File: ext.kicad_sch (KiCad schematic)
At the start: 29 parts, among them J4 0826-1X1T-GH-F, U10 LTC6820IUD, U11 LTC6820IUD, U12 LTC6820IUD, U13 LTC6820IUD

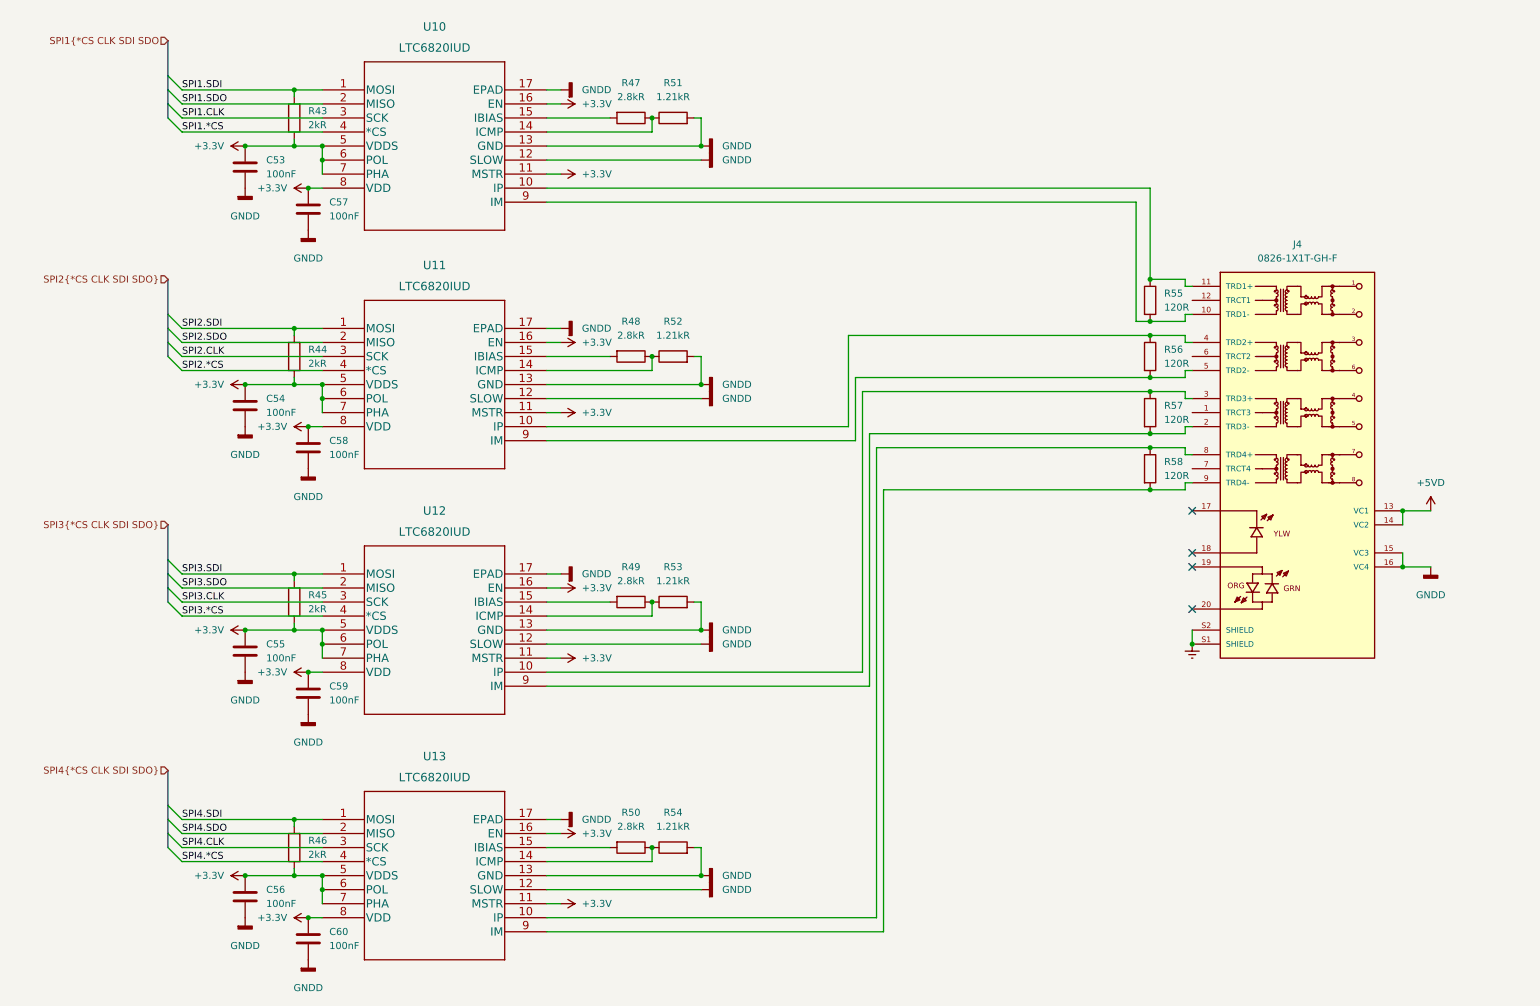
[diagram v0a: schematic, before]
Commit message: Common power stage for field IO
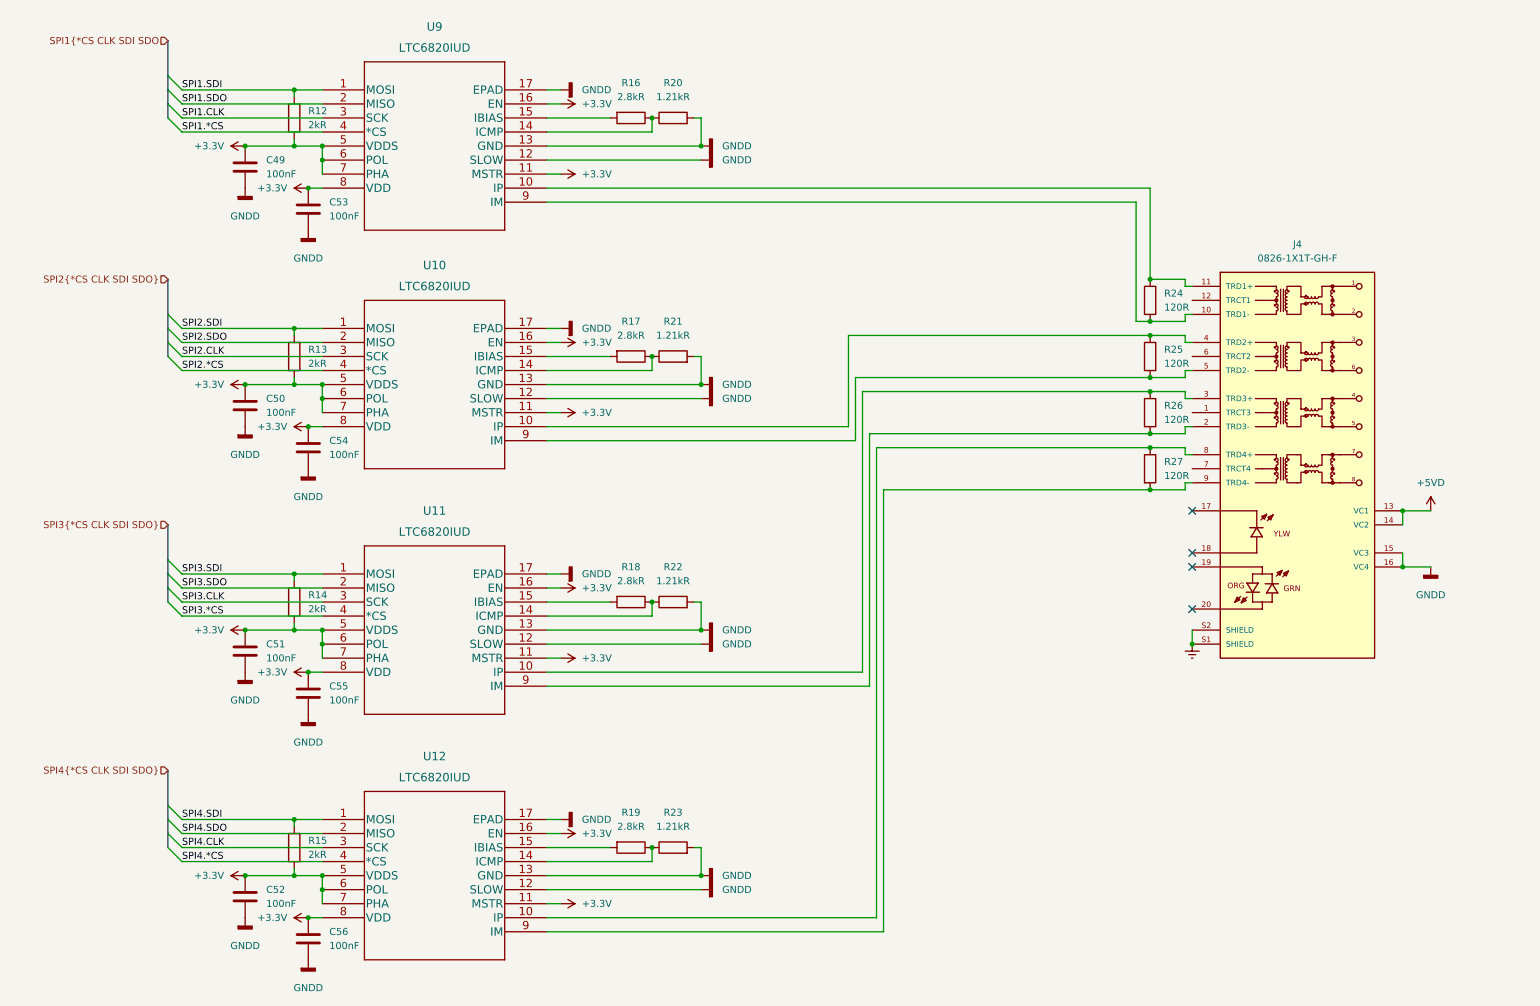
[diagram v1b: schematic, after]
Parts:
- renumbered C53 to C49, C54 to C50, C55 to C51, C56 to C52, C57 to C53, C58 to C54, C59 to C55, C60 to C56, R43 to R12, R44 to R13, R45 to R14, R46 to R15, R47 to R16, R48 to R17, R49 to R18, R50 to R19, R51 to R20, R52 to R21, R53 to R22, R54 to R23, R55 to R24, R56 to R25, R57 to R26, R58 to R27, U11 to U10, U12 to U11, U13 to U12, U10 to U9

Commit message: routing stuff
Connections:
- net TRD1-: now reaches J4.10 (TRD1-), R24.2, U9.9 (IM)
- net TRD1+: now reaches J4.11 (TRD1+), R24.1, U9.10 (IP)
- net TRD3-: now reaches J4.2 (TRD3-), R26.2, U11.9 (IM)
- net TRD3+: now reaches J4.3 (TRD3+), R26.1, U11.10 (IP)
- net TRD2+: now reaches J4.4 (TRD2+), R25.1, U10.10 (IP)
- net TRD2-: now reaches J4.5 (TRD2-), R25.2, U10.9 (IM)
- net TRD4+: now reaches J4.8 (TRD4+), R27.1, U12.10 (IP)
- net TRD4-: now reaches J4.9 (TRD4-), R27.2, U12.9 (IM)
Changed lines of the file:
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@@
+    (effects (font (size 1.27 1.27)) (justify left bottom))
+  )
+  (label "TRD2-" (at 135.89 90.17 0)
     (effects (font (size 1.27 1.27)) (justify left bottom))
   )
@@
     (effects (font (size 1.27 1.27)) (justify left bottom))
   )
+  (label "TRD4+" (at 135.89 176.53 0)
+    (effects (font (size 1.27 1.27)) (justify left bottom))
+  )
   (label "SPI4.*CS" (at 48.26 166.37 0)
     (effects (font (size 1.27 1.27)) (justify left bottom))
@@
   )
   (label "SPI2.SDI" (at 48.26 69.85 0)
+    (effects (font (size 1.27 1.27)) (justify left bottom))
+  )
+  (label "TRD1-" (at 133.35 46.99 0)
+    (effects (font (size 1.27 1.27)) (justify left bottom))
+  )
+  (label "TRD2+" (at 135.89 87.63 0)
     (effects (font (size 1.27 1.27)) (justify left bottom))
   )
@@
     (effects (font (size 1.27 1.27)) (justify left bottom))
   )
+  (label "TRD1+" (at 133.35 44.45 0)
+    (effects (font (size 1.27 1.27)) (justify left bottom))
+  )
+  (label "TRD3+" (at 137.16 132.08 0)
+    (effects (font (size 1.27 1.27)) (justify left bottom))
+  )
+  (label "TRD4-" (at 135.89 179.07 0)
+    (effects (font (size 1.27 1.27)) (justify left bottom))
+  )
   (label "SPI3.CLK" (at 48.26 119.38 0)
     (effects (font (size 1.27 1.27)) (justify left bottom))
@@
     (effects (font (size 1.27 1.27)) (justify left bottom))
   )
+  (label "TRD3-" (at 137.16 134.62 0)
+    (effects (font (size 1.27 1.27)) (justify left bottom))
+  )

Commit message: Basic routing done, cheating a bit on the diff + add holes (to be positionned)
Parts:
- U10, U11, U12, U9: footprint Maxim industrial IO:LTC6820IUD -> QFN-16_UD_AA_ADI
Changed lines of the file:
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@@
     (pin "1")
   )
-  (symbol (lib_name "LTC6820IUD_2") (lib_id "Num-IO:LTC6820IUD") (at 73.66 158.75 0) (unit 1)
+  (symbol (lib_id "Num-IO:LTC6820IUD") (at 73.66 158.75 0) (unit 1)
     (in_bom yes) (on_board yes) (fields_autoplaced)
     (property "Reference" "U12" (id 0) (at 93.98 147.32 0)
@@
       (effects (font (size 1.524 1.524)))
     )
-    (property "Footprint" "Maxim industrial IO:LTC6820IUD" (id 2) (at 93.98 152.654 0)
+    (property "Footprint" "QFN-16_UD_AA_ADI" (id 2) (at 93.98 152.654 0)
       (effects (font (size 1.524 1.524)) hide)
     )
@@
     (pin "2")
   )
-  (symbol (lib_name "LTC6820IUD_1") (lib_id "Num-IO:LTC6820IUD") (at 73.66 114.3 0) (unit 1)
+  (symbol (lib_id "Num-IO:LTC6820IUD") (at 73.66 114.3 0) (unit 1)
     (in_bom yes) (on_board yes) (fields_autoplaced)
     (property "Reference" "U11" (id 0) (at 93.98 102.87 0)
@@
       (effects (font (size 1.524 1.524)))
     )
-    (property "Footprint" "Maxim industrial IO:LTC6820IUD" (id 2) (at 93.98 108.204 0)
+    (property "Footprint" "QFN-16_UD_AA_ADI" (id 2) (at 93.98 108.204 0)
       (effects (font (size 1.524 1.524)) hide)
     )
@@
       (effects (font (size 1.524 1.524)))
     )
-    (property "Footprint" "Maxim industrial IO:LTC6820IUD" (id 2) (at 93.98 63.754 0)
+    (property "Footprint" "QFN-16_UD_AA_ADI" (id 2) (at 93.98 63.754 0)
       (effects (font (size 1.524 1.524)) hide)
     )
@@
     (pin "1")
   )
-  (symbol (lib_name "LTC6820IUD_3") (lib_id "Num-IO:LTC6820IUD") (at 73.66 26.67 0) (unit 1)
+  (symbol (lib_id "Num-IO:LTC6820IUD") (at 73.66 26.67 0) (unit 1)
     (in_bom yes) (on_board yes) (fields_autoplaced)
     (property "Reference" "U9" (id 0) (at 93.98 15.24 0)
@@
       (effects (font (size 1.524 1.524)))
     )
-    (property "Footprint" "Maxim industrial IO:LTC6820IUD" (id 2) (at 93.98 20.574 0)
+    (property "Footprint" "QFN-16_UD_AA_ADI" (id 2) (at 93.98 20.574 0)
       (effects (font (size 1.524 1.524)) hide)
     )

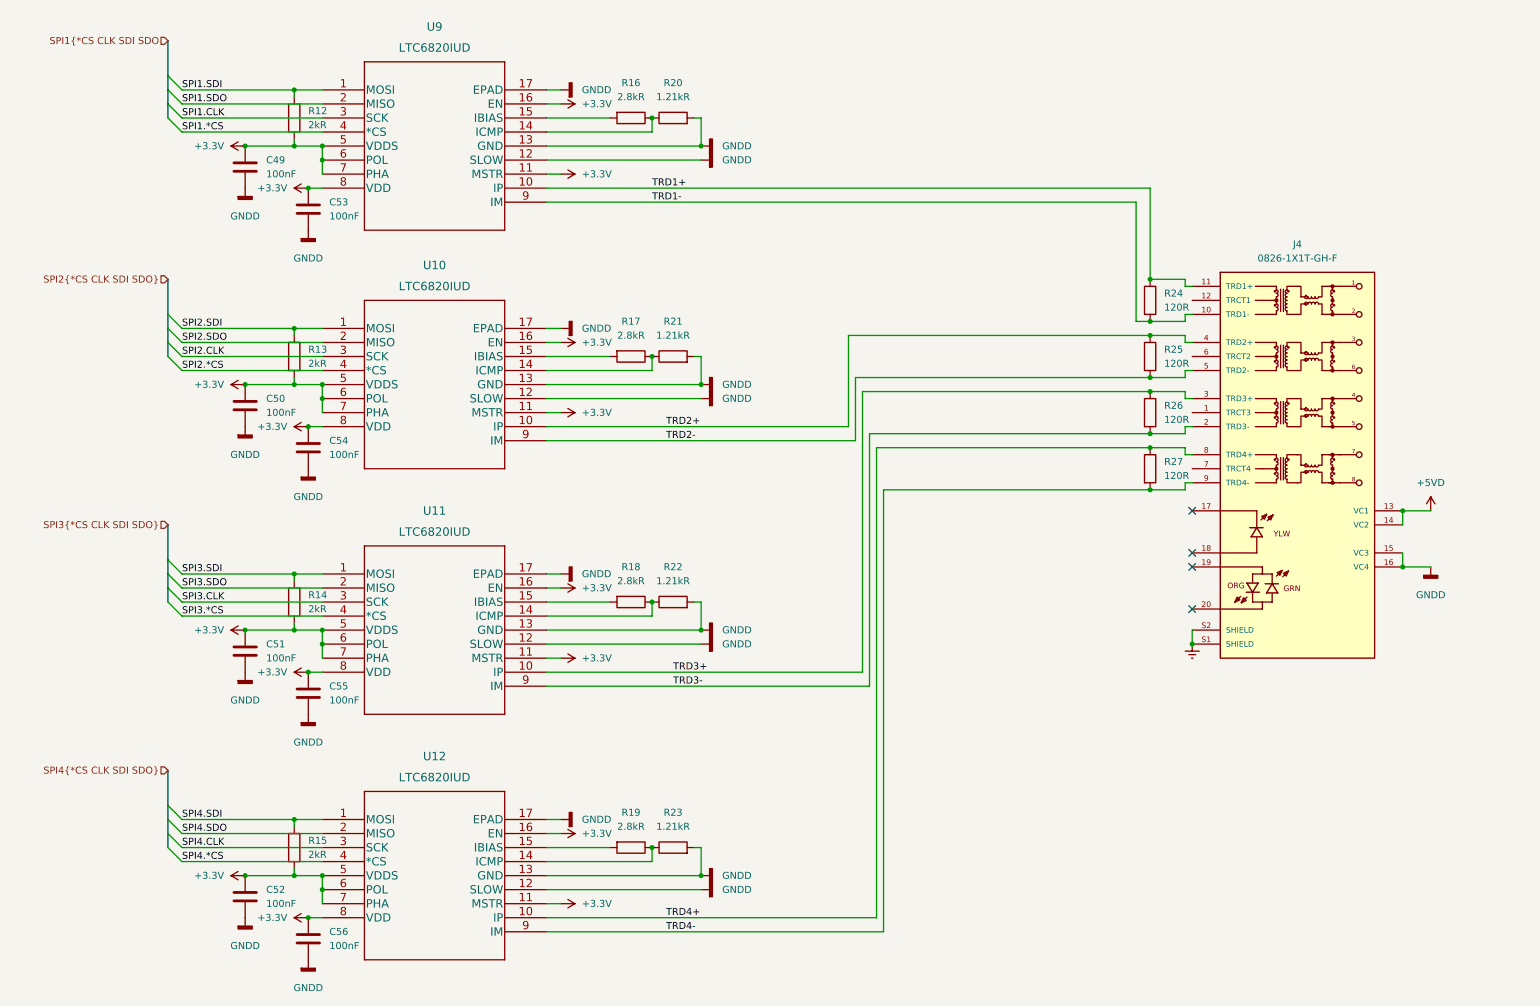
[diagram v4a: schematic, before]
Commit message: change package QFN => MSOP
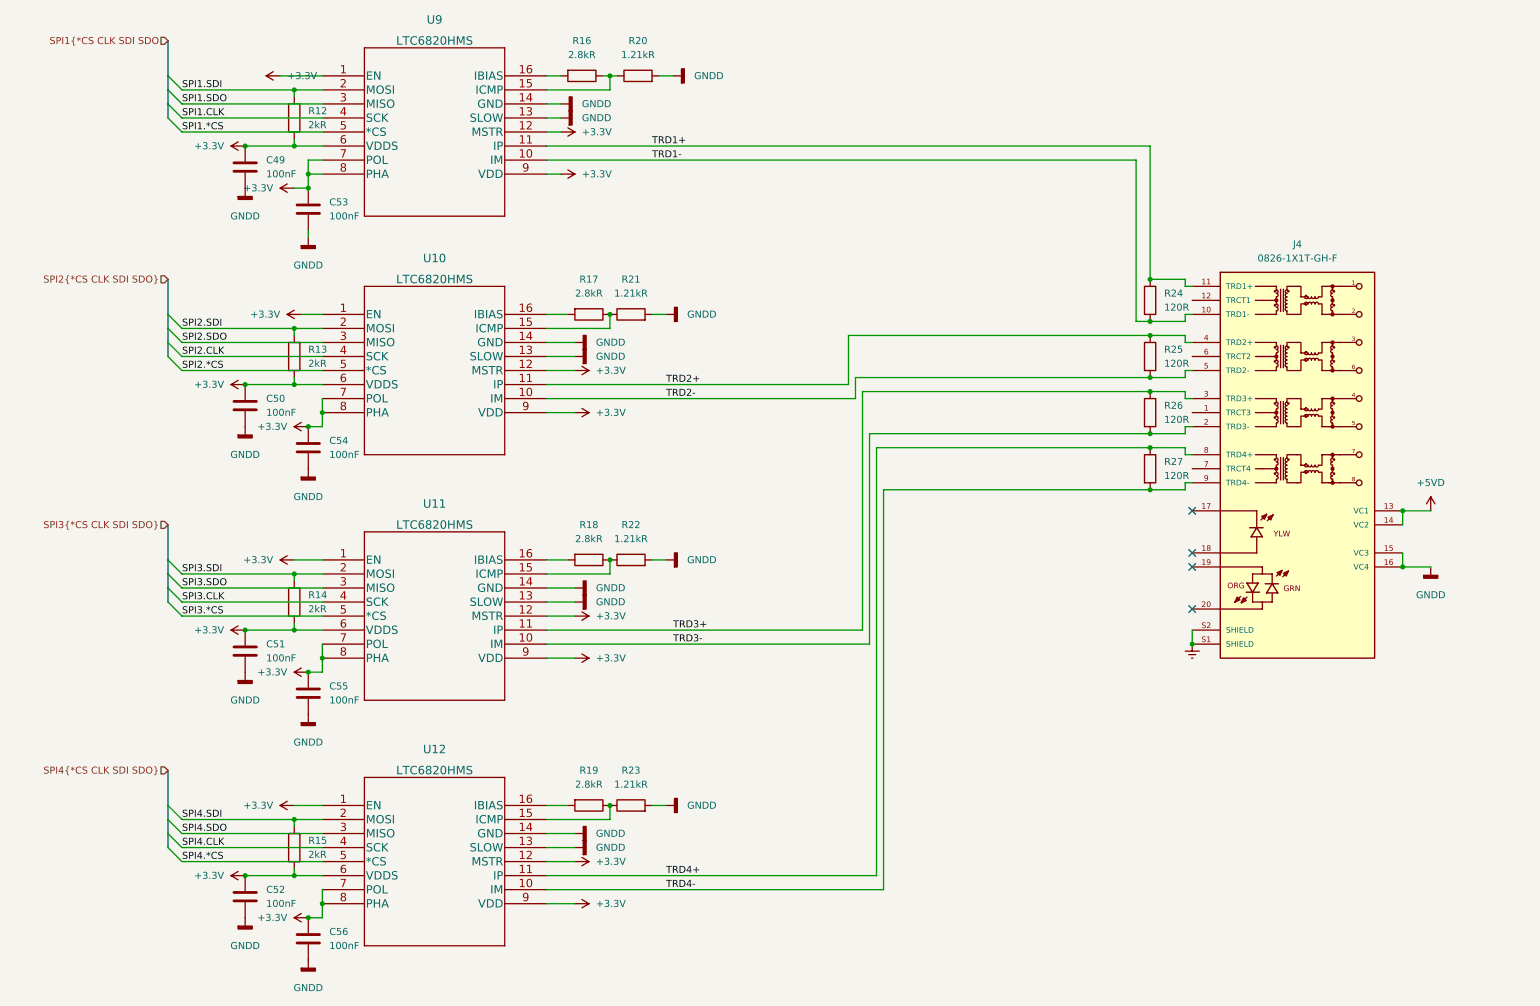
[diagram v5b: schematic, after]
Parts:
- removed U10, U11, U12, U9: LTC6820IUD, QFN-16_UD_AA_ADI, symbol Num-IO:LTC6820IUD
- added U10, U11, U12, U9: LTC6820HMS, Package_SO:MSOP-16_3x4.039mm_P0.5mm, symbol Num-IO:LTC6820HMS
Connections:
- net +3.3V: now also U10.1 (EN), U10.12 (MSTR), U10.6 (VDDS), U10.7 (POL), U10.8 (PHA), U10.9 (VDD), U11.1 (EN), U11.12 (MSTR), U11.6 (VDDS), U11.7 (POL), U11.8 (PHA), U11.9 (VDD), U12.1 (EN), U12.12 (MSTR), U12.6 (VDDS), U12.7 (POL), U12.8 (PHA), U12.9 (VDD), U9.1 (EN), U9.12 (MSTR), U9.6 (VDDS), U9.7 (POL), U9.8 (PHA), U9.9 (VDD)
- net GNDD: now also U10.13 (SLOW), U10.14 (GND), U11.13 (SLOW), U11.14 (GND), U12.13 (SLOW), U12.14 (GND), U9.13 (SLOW), U9.14 (GND)
- net SPI1.*CS: now also U9.5 (*CS)
- net SPI1.CLK: now also U9.4 (SCK)
- net SPI1.SDI: now also U9.2 (MOSI)
- net SPI1.SDO: now also U9.3 (MISO)
- net SPI2.*CS: now also U10.5 (*CS)
- net SPI2.CLK: now also U10.4 (SCK)
- net SPI2.SDI: now also U10.2 (MOSI)
- net SPI2.SDO: now also U10.3 (MISO)
- net SPI3.*CS: now also U11.5 (*CS)
- net SPI3.CLK: now also U11.4 (SCK)
- net SPI3.SDI: now also U11.2 (MOSI)
- net SPI3.SDO: now also U11.3 (MISO)
- net SPI4.*CS: now also U12.5 (*CS)
- net SPI4.CLK: now also U12.4 (SCK)
- net SPI4.SDI: now also U12.2 (MOSI)
- net SPI4.SDO: now also U12.3 (MISO)
- net TRD1+: now also U9.11 (IP)
- net TRD1-: now also U9.10 (IM)
- net TRD2+: now also U10.11 (IP)
- net TRD2-: now also U10.10 (IM)
- net TRD3+: now also U11.11 (IP)
- net TRD3-: now also U11.10 (IM)
- net TRD4+: now also U12.11 (IP)
- net TRD4-: now also U12.10 (IM)
- net at R18.1, R22.1: now also U11.15 (ICMP)
- net at R18.2: now also U11.16 (IBIAS)
- net at R17.1, R21.1: now also U10.15 (ICMP)
- net at R19.1, R23.1: now also U12.15 (ICMP)
- net at R19.2: now also U12.16 (IBIAS)
- net at R17.2: now also U10.16 (IBIAS)
- net at R16.1, R20.1: now also U9.15 (ICMP)
- net at R16.2: now also U9.16 (IBIAS)
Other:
- moved on the sheet: R16, R17, R20, R21

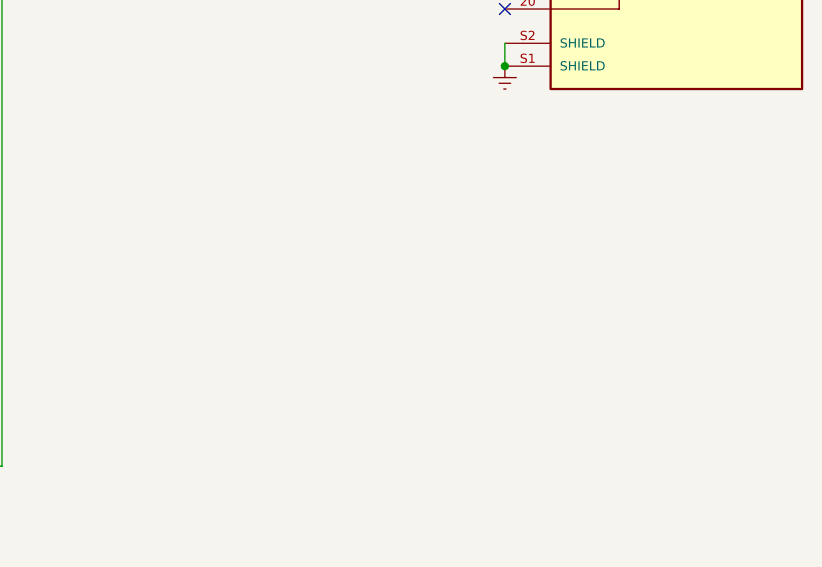
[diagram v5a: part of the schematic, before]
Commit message: add missing LDO for 3.3V
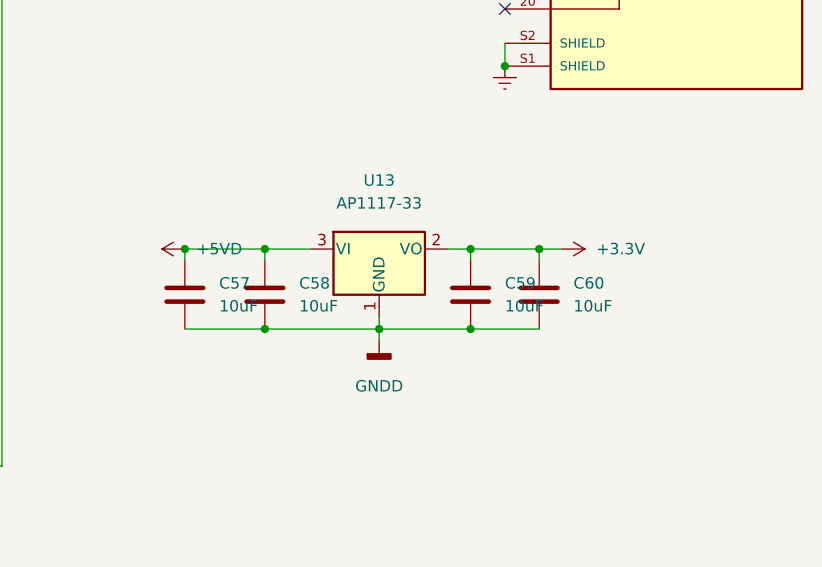
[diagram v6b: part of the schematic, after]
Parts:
- added C57, C58, C59, C60: 10uF, Capacitor_SMD:C_1206_3216Metric, symbol Device:C
- added U13: AP1117-33, Package_TO_SOT_SMD:SOT-223-3_TabPin2, symbol Regulator_Linear:AZ1117-3.3
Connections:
- net +3.3V: now also C59.1, C60.1, U13.2 (VO)
- net +5VD: now also C57.1, C58.1, U13.3 (VI)
- net GNDD: now also C57.2, C58.2, C59.2, C60.2, U13.1 (GND)
